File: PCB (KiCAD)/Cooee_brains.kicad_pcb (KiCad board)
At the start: 2 copper layers, 66.8 x 151.3 mm, 49 parts, among them J1 USB4105-GF-A, J2 Conn_Coaxial, J3 503398-1892, J4 Conn_01x14_Socket, J5 Conn_01x02_Pin, J6 Conn_Coaxial, J7 Conn_01x04_Pin, J9 Conn_01x05_Socket, SW1 Prog, SW2 Reset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

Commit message: motherboard PCB work
motherboard PCB work
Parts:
- added C10: 10uF, Capacitor_SMD:C_0805_2012Metric, B.Cu at (190.3, 58.7)
- added C11: 10uF, Capacitor_SMD:C_0805_2012Metric, B.Cu at (173.6, 64.3)
- added D4: LED, Capacitor_SMD:C_0805_2012Metric, B.Cu at (187.2, 70.0)
- added D5: LED, Capacitor_SMD:C_0805_2012Metric, B.Cu at (185.1, 70.1)
- added H4: MountingHole_Pad_MP, MountingHole:MountingHole_3.2mm_M3_DIN965_Pad_TopBottom, F.Cu at (181.6, 59.9)
- added JP1: SolderJumper_2_Open, Jumper:SolderJumper-2_P1.3mm_Open_RoundedPad1.0x1.5mm, B.Cu at (144.8, 111.4)
- added JP2: SolderJumper_2_Open, Jumper:SolderJumper-2_P1.3mm_Open_RoundedPad1.0x1.5mm, B.Cu at (144.8, 108.8)
- added JP3: SolderJumper_2_Open, Jumper:SolderJumper-2_P1.3mm_Open_RoundedPad1.0x1.5mm, B.Cu at (161.5, 106.6)
- added JP4: SolderJumper_2_Open, Jumper:SolderJumper-2_P1.3mm_Open_RoundedPad1.0x1.5mm, B.Cu at (161.5, 104.0)
- added JP5: SolderJumper_2_Open, Jumper:SolderJumper-2_P1.3mm_Open_RoundedPad1.0x1.5mm, B.Cu at (175.0, 72.7)
- added R15: R2, Capacitor_SMD:C_0805_2012Metric_Pad1.18x1.45mm_HandSolder, B.Cu at (172.2, 74.8)
- added R16: R1, Capacitor_SMD:C_0805_2012Metric_Pad1.18x1.45mm_HandSolder, B.Cu at (172.2, 70.4)
- added R17: 1000, Capacitor_SMD:C_0805_2012Metric_Pad1.18x1.45mm_HandSolder, B.Cu at (185.1, 66.3)
- added R18: 1000, Capacitor_SMD:C_0805_2012Metric_Pad1.18x1.45mm_HandSolder, B.Cu at (187.2, 66.4)
- added R19: 10kΩ, Capacitor_SMD:C_0805_2012Metric_Pad1.18x1.45mm_HandSolder, B.Cu at (181.3, 100.9)
- added R20: 10kΩ, Capacitor_SMD:C_0805_2012Metric_Pad1.18x1.45mm_HandSolder, B.Cu at (170.6, 102.8)
- added RProg1: 330, Capacitor_SMD:C_0805_2012Metric_Pad1.18x1.45mm_HandSolder, B.Cu at (171.6, 67.1)
- added TH1: Thermistor_NTC, Resistor_SMD:R_0805_2012Metric_Pad1.20x1.40mm_HandSolder, B.Cu at (168.9, 55.5)
- added U7: TP4056, USB4105-GF-A (1):SOP127P600X175-9N, B.Cu at (177.9, 68.2)
- D1, R12, R13, R14: moved to B.Cu
- moved R12 134.7 mm to (130.6, 124.4)
- moved C8 124.8 mm to (140.5, 99.2), turned to -90 degrees
- moved C6 122.3 mm to (142.6, 99.1), turned to 90 degrees
- moved C9 121.9 mm to (140.6, 103.2), turned to -90 degrees
- moved C7 119.9 mm to (144.7, 99.1), turned to 90 degrees
- moved R11 118.6 mm to (146.9, 97.5), turned to -90 degrees
- moved R8 115.3 mm to (149.1, 98.4), turned to -90 degrees
- moved U6 112.6 mm to (147.5, 104.2), turned to 0 degrees
- moved C5 107.6 mm to (152.3, 103.2), turned to -90 degrees
- moved R13 95.2 mm to (138.5, 75.5), turned to -135 degrees
- moved R14 94.7 mm to (136.2, 73.2), turned to -135 degrees
- moved SW2 77.5 mm to (158.4, 123.1), turned to 180 degrees
- moved D1 77.3 mm to (175.4, 83.1), turned to 180 degrees
- moved R10 69.2 mm to (165.7, 121.5)
- moved C4 69.2 mm to (163.3, 121.8)
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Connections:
- J5 pad 1: SPEAKER- -> SPEAKER+
- J5 pad 2: SPEAKER+ -> SPEAKER-
- U2 pad 13: MIC_LRCK -> Net-(JP1-A)
- U2 pad 14: MIC_DOUT -> Net-(JP2-A)
- U2 pad 16: unconnected-(U2-IO46-Pad16) -> Net-(U2-IO46)
- U2 pad 26: unconnected-(U2-IO45-Pad26) -> Net-(U2-IO45)
- U3 pad 7: VDD -> 3.3V
- U3 pad 8: VDD -> 3.3V
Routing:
- net 3.3V: track 15.7 -> 90.3 mm, vias 0 -> 1
- net Batt+: track 2.10 -> 65.6 mm
- net KEEB_INT: track 0.00 -> 54.8 mm, vias 0 -> 2
- net 5V: track 9.08 -> 58.3 mm, vias 0 -> 3
- net Interface_Tx: track 1.59 -> 44.4 mm, vias 0 -> 2
- net Interface_Rx: track 1.67 -> 43.9 mm, vias 0 -> 2
- net SHARED_MOSI: track 0.00 -> 39.6 mm
- net SHARED_MISO: track 0.00 -> 38.2 mm
- net SHARED_CLCK: track 0.00 -> 36.9 mm
- net Net-(JP5-B): track 0.00 -> 24.4 mm, vias 0 -> 2
- net KEEB_SCL: track 0.00 -> 14.7 mm
- net KEEB_D: track 0.00 -> 11.5 mm
- net USB_DP: track 3.69 -> 15.0 mm, vias 0 -> 2
- net GND: track 9.33 -> 20.2 mm, vias 0 -> 6
- net Net-(U7-~{STDBY}): track 0.00 -> 10.4 mm
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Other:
- board size 66.8 x 151.3 mm -> 66.8 x 148.9 mm
- board text removed: "GPS"

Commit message: trying to figure out the dang i2s device configurations
trying to figure out the dang i2s device configurations
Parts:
- moved R20 1.31 mm to (169.6, 103.7), turned to 180 degrees
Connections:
- U2 pad 10: KEEB_SCL -> Display_MISO
- U2 pad 11: MIC_BCLK -> Display_LED_BacklightEN
- U2 pad 12: Display_MOSI -> Display_SCK
- U2 pad 17: Display_SCK -> Display_MOSI
- U2 pad 18: Display_LED_BacklightEN -> Display_DC
- U2 pad 19: Display_MISO -> Display_RST
- U2 pad 20: SPKR_BCLK -> Display_CS
- U2 pad 29: SHARED_MOSI -> unconnected-(U2-IO36-Pad29)
- U2 pad 30: SHARED_MISO -> unconnected-(U2-IO37-Pad30)
- U2 pad 31: SHARED_CLCK -> unconnected-(U2-IO38-Pad31)
- U2 pad 38: KEEB_INT -> unconnected-(U2-IO2-Pad38)
- U2 pad 4: KEEB_D -> MICRO_SD_CS
- U2 pad 5: Display_CS -> T_IRQ
- U2 pad 6: Display_RST -> SHARED_MISO
- U2 pad 7: Display_DC -> SHARED_MOSI
- U2 pad 9: T_IRQ -> SHARED_CLCK
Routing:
- net 3.3V: track 90.3 -> 227.8 mm, vias 1 -> 4
- net SHARED_MISO: track 38.2 -> 111.2 mm, vias 0 -> 2
- net SHARED_MOSI: track 39.6 -> 108.6 mm, vias 0 -> 3
- net SHARED_CLCK: track 36.9 -> 98.5 mm, vias 0 -> 2
- net T_IRQ: track 0.00 -> 43.2 mm
- net T_CS: track 0.00 -> 36.9 mm
- net Display_MISO: track 0.00 -> 32.6 mm
- net Display_LED_BacklightEN: track 0.00 -> 31.8 mm
- net Display_SCK: track 0.00 -> 30.9 mm
- net GND: track 20.2 -> 46.3 mm, vias 6 -> 22
- net MICRO_SD_CS: track 0.00 -> 25.9 mm, vias 0 -> 2
- net Batt+: track 65.6 -> 43.0 mm, vias 0 -> 2
- net Display_MOSI: track 0.00 -> 22.3 mm
- net Display_DC: track 0.00 -> 21.7 mm
- net Display_RST: track 0.00 -> 21.1 mm
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
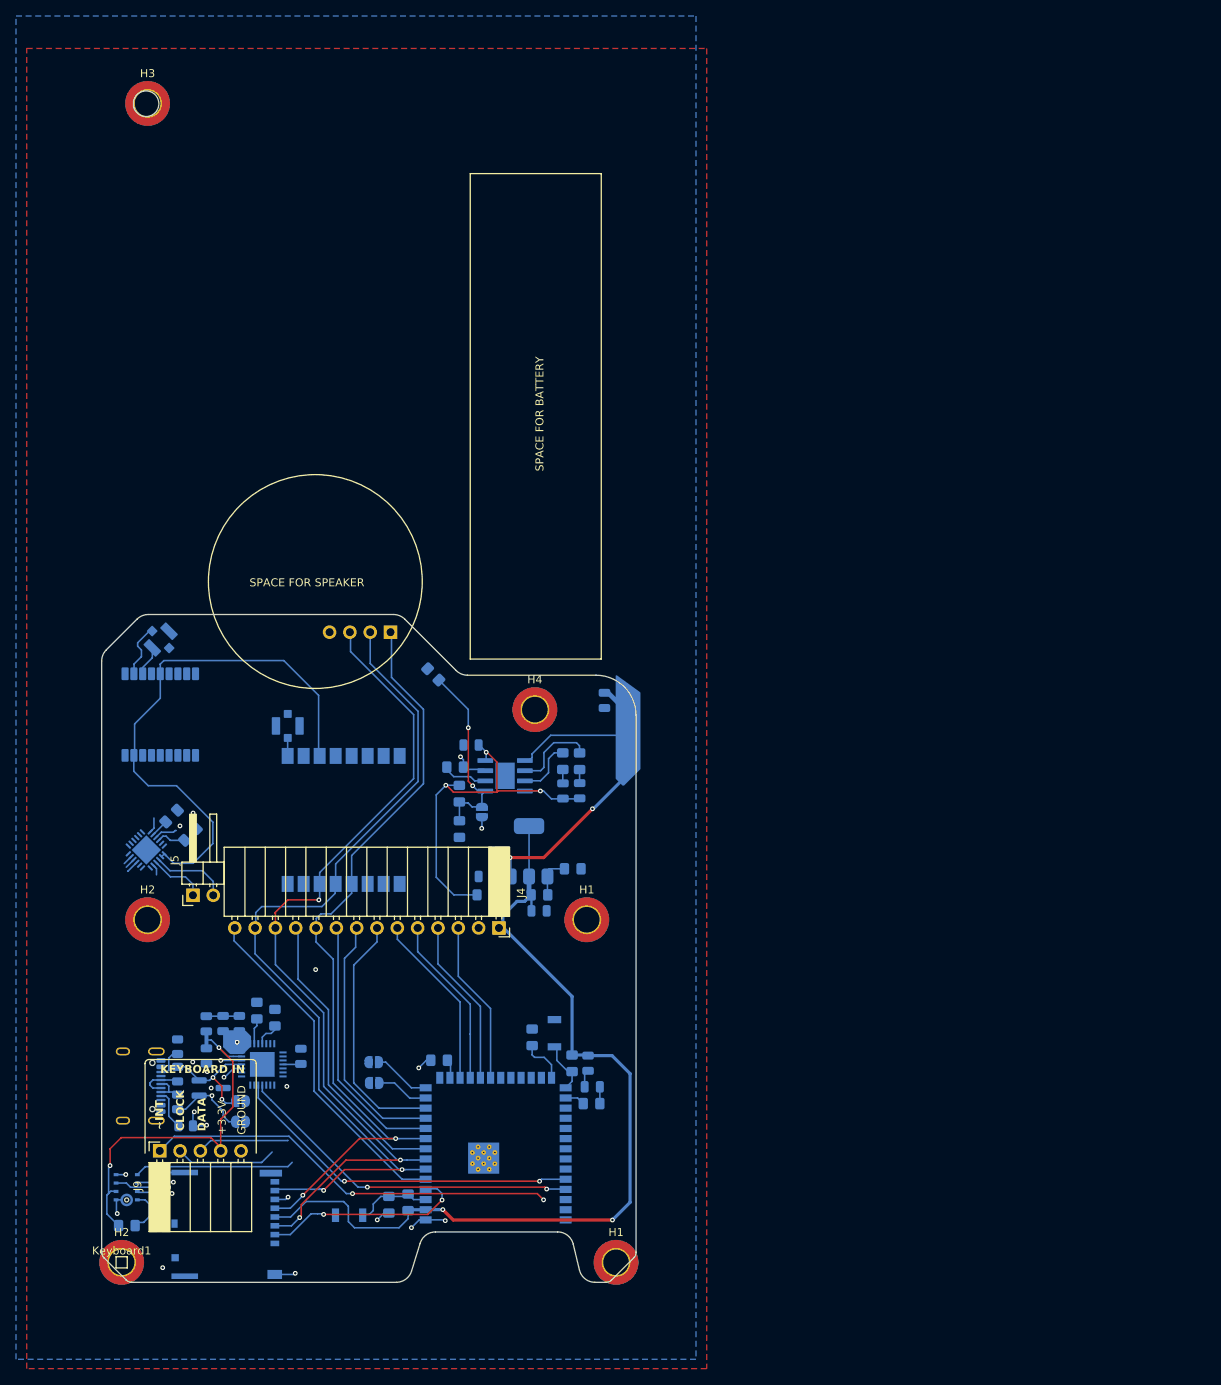
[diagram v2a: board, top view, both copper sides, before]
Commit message: centred the USB port and screen properly
centred the USB port and screen properly. trying to implement compressed audio over radio but compression function started throwing stack overflow
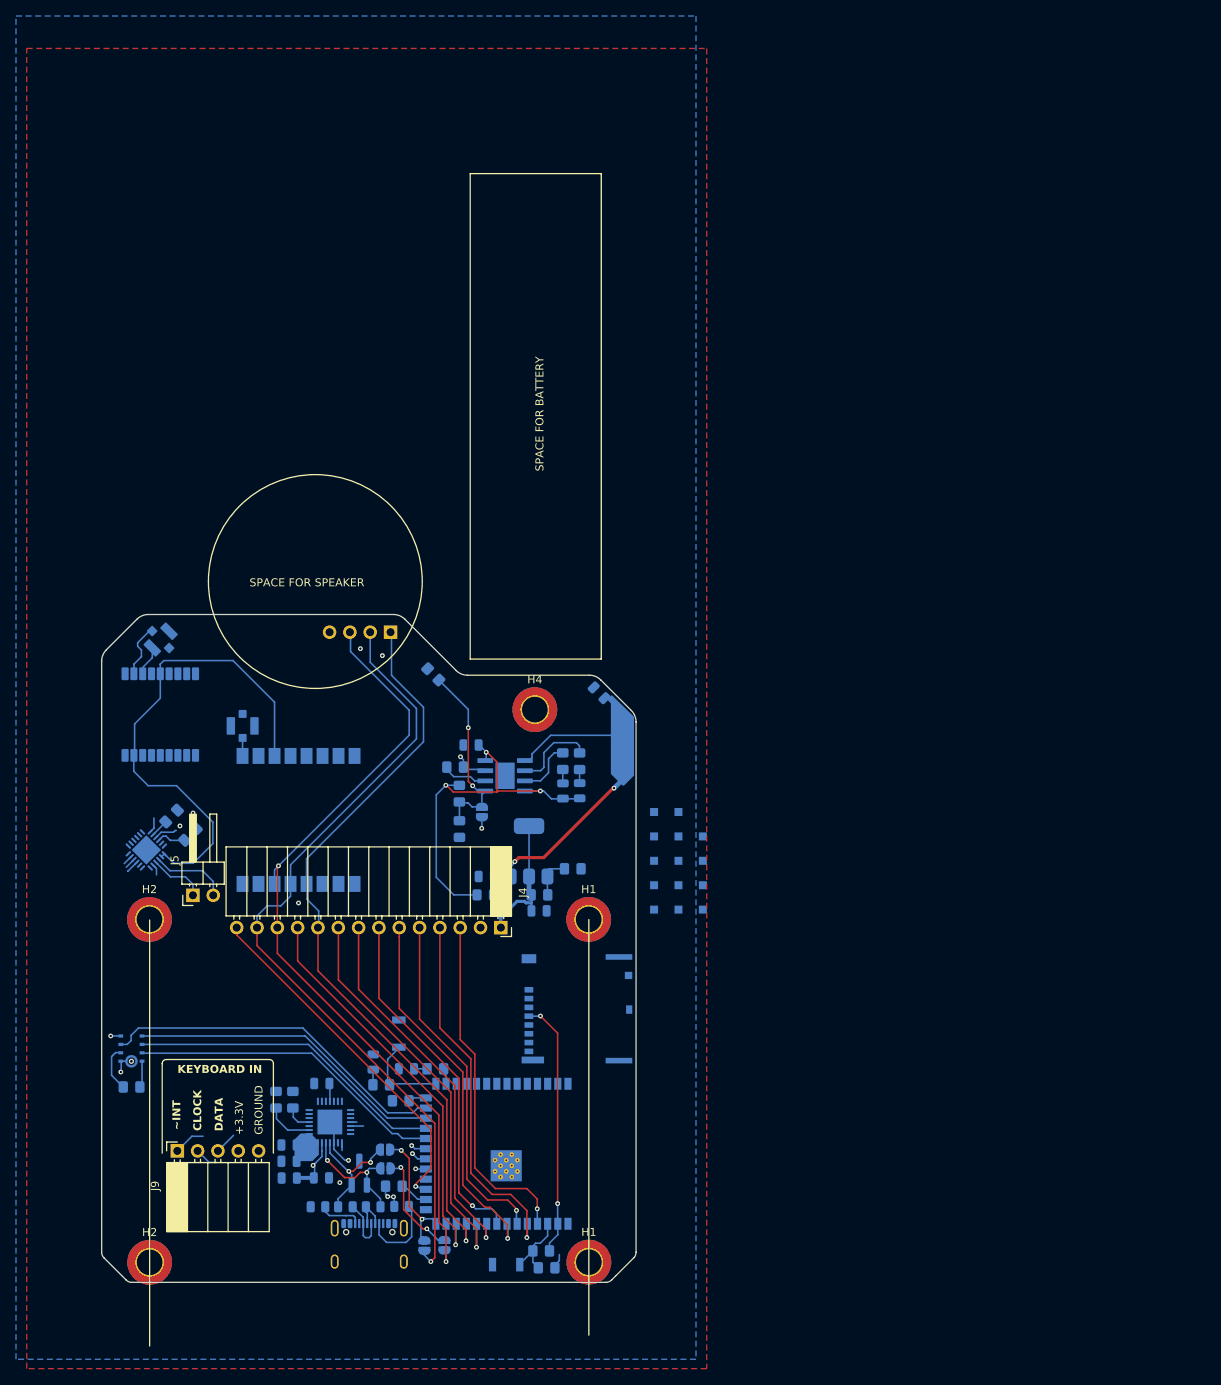
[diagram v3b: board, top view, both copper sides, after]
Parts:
- removed H3: MountingHole_Pad_MP, MountingHole:MountingHole_3.2mm_M3_DIN965_Pad_TopBottom
- removed Keyboard1: Keyboard, TestPoint:TestPoint_Pad_1.0x1.0mm
- added TP1: TestPoint, TestPoint:TestPoint_Pad_1.0x1.0mm, B.Cu at (196.5, 84.9)
- added TP10: TestPoint, TestPoint:TestPoint_Pad_1.0x1.0mm, B.Cu at (199.6, 72.7)
- added TP11: TestPoint, TestPoint:TestPoint_Pad_1.0x1.0mm, B.Cu at (202.6, 84.9)
- added TP12: TestPoint, TestPoint:TestPoint_Pad_1.0x1.0mm, B.Cu at (202.6, 81.8)
- added TP13: TestPoint, TestPoint:TestPoint_Pad_1.0x1.0mm, B.Cu at (202.6, 78.8)
- added TP14: TestPoint, TestPoint:TestPoint_Pad_1.0x1.0mm, B.Cu at (202.6, 75.8)
- added TP2: TestPoint, TestPoint:TestPoint_Pad_1.0x1.0mm, B.Cu at (196.5, 81.8)
- added TP3: TestPoint, TestPoint:TestPoint_Pad_1.0x1.0mm, B.Cu at (196.5, 78.8)
- added TP4: TestPoint, TestPoint:TestPoint_Pad_1.0x1.0mm, B.Cu at (196.5, 75.8)
- added TP5: TestPoint, TestPoint:TestPoint_Pad_1.0x1.0mm, B.Cu at (196.5, 72.7)
- added TP6: TestPoint, TestPoint:TestPoint_Pad_1.0x1.0mm, B.Cu at (199.6, 84.9)
- added TP7: TestPoint, TestPoint:TestPoint_Pad_1.0x1.0mm, B.Cu at (199.6, 81.8)
- added TP8: TestPoint, TestPoint:TestPoint_Pad_1.0x1.0mm, B.Cu at (199.6, 78.8)
- added TP9: TestPoint, TestPoint:TestPoint_Pad_1.0x1.0mm, B.Cu at (199.6, 75.8)
- moved J3 50.7 mm to (186.5, 97.3), turned to -90 degrees
- moved J1 36.3 mm to (160.9, 127.8), turned to 180 degrees
- moved R2 28.8 mm to (164.9, 122.0), turned to 180 degrees
- moved R4 27.7 mm to (161.4, 122.0), turned to 0 degrees
- moved C3 26.9 mm to (161.4, 104.0), turned to -90 degrees
- moved R3 26.7 mm to (157.9, 122.0), turned to 180 degrees
- moved R5 26.6 mm to (154.5, 122.0), turned to 180 degrees
- moved R9 24.0 mm to (162.4, 106.8), turned to 0 degrees
- moved JP4 23.8 mm to (167.8, 126.9), turned to -90 degrees
- moved D74 23.3 mm to (165.5, 104.8)
- moved JP3 22.1 mm to (170.3, 126.8), turned to -90 degrees
- moved C8 21.9 mm to (150.9, 118.5), turned to 0 degrees
- moved D72 21.4 mm to (159.7, 117.8), turned to 90 degrees
- moved C4 21.2 mm to (183.1, 129.7), turned to 0 degrees
- moved C9 21.0 mm to (154.9, 118.4), turned to 0 degrees
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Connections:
- JP3 pad 2: MIC_LRCK -> SHARED_MOSI
- JP4 pad 2: MIC_DOUT -> SHARED_MISO
- U2 pad 11: Display_LED_BacklightEN -> SHARED_CLCK
- U2 pad 12: Display_SCK -> T_CS
- U2 pad 17: Display_MOSI -> T_IRQ
- U2 pad 18: Display_DC -> unconnected-(U2-IO10-Pad18)
- U2 pad 19: Display_RST -> unconnected-(U2-IO11-Pad19)
- U2 pad 20: Display_CS -> unconnected-(U2-IO12-Pad20)
- U2 pad 22: SPKR_LRCK -> MIC_LRCK
- U2 pad 23: MIC_EN -> MIC_DOUT
- U2 pad 24: unconnected-(U2-IO47-Pad24) -> MIC_BCLK
- U2 pad 25: LoRa_Select -> MIC_EN
- U2 pad 30: unconnected-(U2-IO37-Pad30) -> MICRO_SD_CS
- U2 pad 31: unconnected-(U2-IO38-Pad31) -> SPKR_BCLK
- U2 pad 4: MICRO_SD_CS -> Display_CS
- U2 pad 5: T_IRQ -> Display_RST
- U2 pad 6: SHARED_MISO -> Display_DC
- U2 pad 7: SHARED_MOSI -> Display_MOSI
- U2 pad 8: T_CS -> Display_SCK
- U2 pad 9: SHARED_CLCK -> Display_LED_BacklightEN
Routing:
- net 3.3V: track 227.8 -> 125.5 mm, vias 4 -> 3
- net KEEB_INT: track 52.0 -> 4.01 mm, vias 2 -> 0
- net Interface_Rx: track 43.9 -> 0.79 mm, vias 2 -> 0
- net Interface_Tx: track 44.4 -> 1.61 mm, vias 2 -> 0
- net MIC_EN: track 6.79 -> 44.0 mm, vias 1 -> 0
- net MIC_LRCK: track 4.46 -> 39.9 mm, vias 1 -> 0
- net MIC_DOUT: track 4.70 -> 39.8 mm, vias 1 -> 0
- net MICRO_SD_CS: track 25.9 -> 0.00 mm, vias 2 -> 0
- net Display_RST: track 21.1 -> 46.5 mm, vias 0 -> 1
- net Display_MOSI: track 22.3 -> 47.0 mm, vias 0 -> 1
- net Display_CS: track 20.4 -> 43.3 mm, vias 0 -> 1
- net Display_DC: track 21.7 -> 43.8 mm, vias 0 -> 1
- net MIC_BCLK: track 20.0 -> 39.7 mm
- net Display_MISO: track 32.6 -> 50.0 mm, vias 0 -> 1
- net GND: track 46.3 -> 29.3 mm, vias 22 -> 13
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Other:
- board size 66.8 x 148.9 mm -> 66.8 x 83.5 mm
- board text added: "BATTERY POSITIVE + --->"

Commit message: got past the stack overflow when encoding audio samples
got past the stack overflow when encoding audio samples
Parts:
- removed the H1 at (188.3, 86.1)
- removed the H2 at (133.4, 86.1)
- removed H4: MountingHole_Pad_MP, MountingHole:MountingHole_3.2mm_M3_DIN965_Pad_TopBottom
- added BT1: 628, USB4105-GF-A (1):BAT_628, B.Cu at (179.3, 68.7)
- moved J6 60.9 mm to (191.1, 74.6), turned to 90 degrees
- moved U5 58.3 mm to (189.5, 82.8)
- moved R14 56.2 mm to (144.4, 128.8), turned to 0 degrees
- moved R13 49.8 mm to (142.5, 125.2), turned to 0 degrees
- moved U3 49.3 mm to (147.8, 124.4), turned to 45 degrees
- moved J5 37.8 mm to (129.9, 119.8), turned to 0 degrees
- moved J7 35.0 mm to (151.8, 83.2)
- moved TH1 34.3 mm to (172.3, 89.7), turned to 180 degrees
- moved U8 31.6 mm to (137.5, 101.7)
- moved U1 30.5 mm to (155.4, 94.3), turned to 180 degrees
- moved J2 30.2 mm to (131.5, 89.0)
- moved R7 27.1 mm to (161.7, 91.1)
- moved TP1 27.0 mm to (214.3, 64.7)
- moved TP11 27.0 mm to (220.4, 64.7)
- moved TP14 27.0 mm to (220.4, 55.5)
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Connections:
- U2 pad 12: T_CS -> unconnected-(U2-IO8-Pad12)
- U2 pad 17: T_IRQ -> unconnected-(U2-IO9-Pad17)
- U2 pad 18: unconnected-(U2-IO10-Pad18) -> KEEB_D
- U2 pad 19: unconnected-(U2-IO11-Pad19) -> KEEB_INT
- U2 pad 20: unconnected-(U2-IO12-Pad20) -> SPKR_LRCK
- U2 pad 29: unconnected-(U2-IO36-Pad29) -> LoRa_Select
- U2 pad 38: unconnected-(U2-IO2-Pad38) -> KEEB_SCL
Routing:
- net SHARED_MOSI: track 101.3 -> 43.2 mm, vias 2 -> 0
- net T_CS: track 50.6 -> 0.13 mm, vias 1 -> 0
- net T_IRQ: track 44.7 -> 0.00 mm, vias 1 -> 0
- net LoRa_Select: track 0.00 -> 44.3 mm, vias 0 -> 2
- net KEEB_D: track 3.19 -> 37.8 mm, vias 0 -> 2
- net Batt+: track 42.2 -> 12.0 mm, vias 2 -> 0
- net Interface_Tx: track 1.61 -> 28.8 mm, vias 0 -> 4
- net GPS_SlaveIn: track 0.00 -> 26.2 mm
- net GPS_SlaveOut: track 0.00 -> 26.0 mm
- net Interface_Rx: track 0.79 -> 26.6 mm, vias 0 -> 2
- net GPS_On/OFF: track 0.00 -> 23.7 mm, vias 0 -> 2
- net MIC_EN: track 44.0 -> 20.9 mm
- net GPS_RST: track 0.00 -> 22.8 mm, vias 0 -> 2
- net MIC_BCLK: track 39.7 -> 17.0 mm
- net MIC_DOUT: track 39.8 -> 17.4 mm
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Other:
- board size 66.8 x 83.5 mm -> 66.8 x 65.3 mm
- board text added: "GPS Antenna"
- board text added: "LoRa Antenna"
- board text added: "Micro_SD"

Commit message: pcb work
pcb work
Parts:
- removed TP10, TP2, TP3, TP8, TP9: TestPoint, TestPoint:TestPoint_Pad_1.0x1.0mm
- TP1, TP11, TP12, TP13, TP14, TP4, TP5, TP6, TP7: moved to F.Cu
- moved TP14 100.9 mm to (136.8, 112.0)
- moved TP13 97.1 mm to (139.4, 112.1)
- moved TP12 93.2 mm to (142.0, 112.0)
- moved TP11 89.4 mm to (144.6, 112.0)
- moved TP7 75.4 mm to (170.8, 120.9)
- moved TP5 69.5 mm to (163.2, 99.5)
- moved TP4 66.8 mm to (160.9, 95.7)
- moved TP6 50.6 mm to (178.2, 96.6)
- moved TP1 49.0 mm to (172.4, 90.0), turned to 180 degrees
- moved JP3 2.34 mm to (169.3, 128.9), turned to -135 degrees
- moved BT1 0.76 mm to (178.5, 68.7)
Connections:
- H1 pad 1: (no net) -> GND
- H2 pad 1: (no net) -> GND
- J1 pad S1: (no net) -> GND
- JP3 pad 2: SHARED_MOSI -> SPKR_BCLK
- JP4 pad 2: SHARED_MISO -> SPKR_LRCK
- TP1 pad 1: unconnected-(TP1-Pad1) -> Display_CS
- TP11 pad 1: unconnected-(TP11-Pad1) -> 3.3V
- TP12 pad 1: unconnected-(TP12-Pad1) -> KEEB_D
- TP13 pad 1: unconnected-(TP13-Pad1) -> KEEB_SCL
- TP14 pad 1: unconnected-(TP14-Pad1) -> KEEB_INT
- TP4 pad 1: unconnected-(TP4-Pad1) -> SHARED_MOSI
- TP5 pad 1: unconnected-(TP5-Pad1) -> SHARED_MISO
- TP6 pad 1: unconnected-(TP6-Pad1) -> SHARED_CLCK
- TP7 pad 1: unconnected-(TP7-Pad1) -> SPARE1
- U2 pad 12: unconnected-(U2-IO8-Pad12) -> SPKR_DIN
- U2 pad 17: unconnected-(U2-IO9-Pad17) -> SHARED_MISO
- U2 pad 20: SPKR_LRCK -> LoRa_DIO1
- U2 pad 21: SPKR_DIN -> SPARE1
- U2 pad 31: SPKR_BCLK -> SHARED_MOSI
- U2 pad 41: (no net) -> GND
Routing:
- net GND: track 39.4 -> 103.3 mm, vias 23 -> 72
- net KEEB_SCL: track 3.01 -> 61.9 mm, vias 0 -> 3
- net LoRa_DIO1: track 0.00 -> 57.5 mm, vias 0 -> 2
- net 3.3V: track 145.5 -> 197.6 mm, vias 6 -> 9
- net SHARED_MOSI: track 43.2 -> 85.7 mm, vias 0 -> 1
- net KEEB_INT: track 5.30 -> 43.6 mm
- net Batt+: track 12.0 -> 49.7 mm, vias 0 -> 2
- net SHARED_MISO: track 87.6 -> 118.8 mm, vias 2 -> 3
- net SPKR_DIN: track 3.87 -> 33.0 mm, vias 1 -> 0
- net 5V: track 57.3 -> 85.0 mm, vias 3 -> 9
- net SPKR_BCLK: track 1.37 -> 24.1 mm
- net SPKR_LRCK: track 1.95 -> 24.0 mm, vias 1 -> 0
- net BigSD_CS: track 20.2 -> 0.00 mm
- net (no net): track 0.00 -> 13.7 mm
- net SHARED_CLCK: track 95.1 -> 106.0 mm, vias 1 -> 3
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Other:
- board text added: "ESP32-S3"
- board text added: "LoRa Module"
- board text added: "MicroController"
- board text added: "RA-01H"
- board text added: "SDCard Slot"
